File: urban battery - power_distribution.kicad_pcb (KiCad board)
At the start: 2 copper layers, 88.3 x 71.4 mm, 20 parts, among them J1 FRONT_ACC_OUT, J2 12V_IN, J3 12VHC_OUT_EXTRA, J4 TEL_OUT, J5 REAR_ACC_OUT, J6 MTR_CTRL_OUT, J7 12VLC_OUT_EXTRA, J8 12VLC_OUT_EXTRA, J9 12VLC_OUT_EXTRA

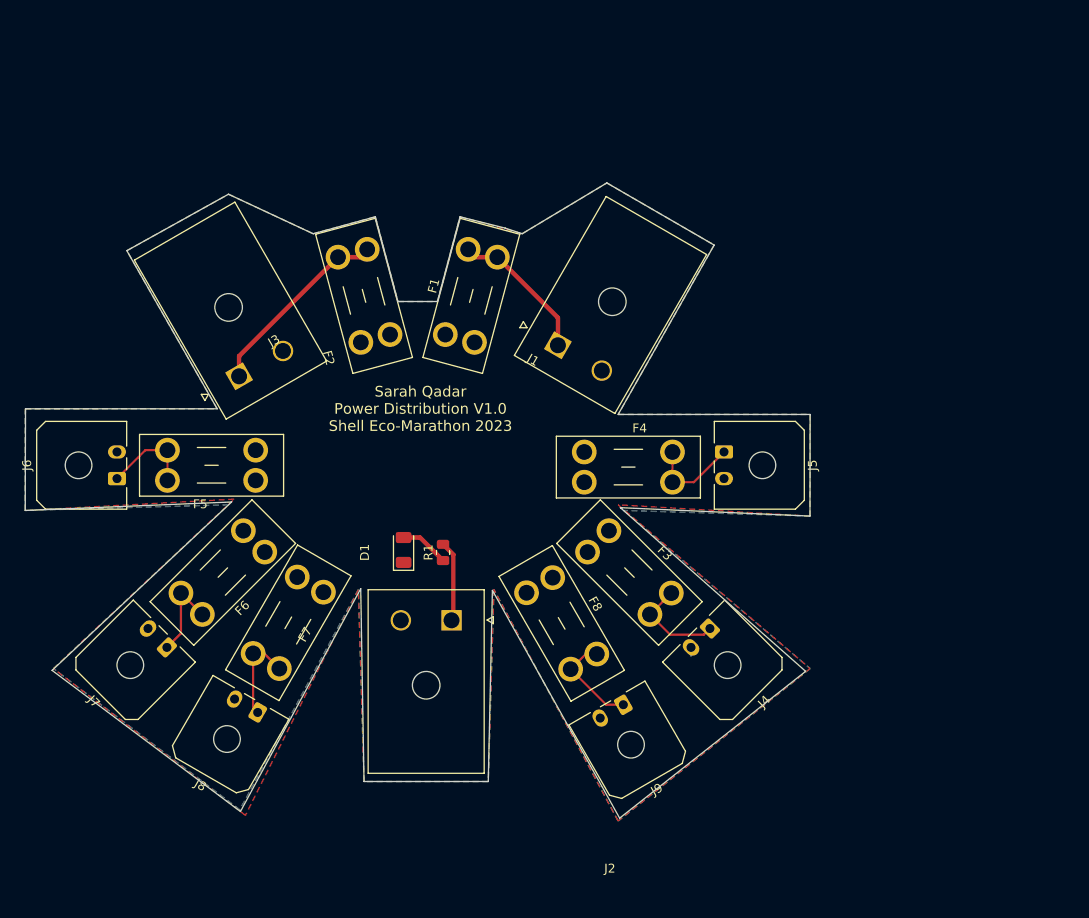
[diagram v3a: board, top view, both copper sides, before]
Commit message: fixed issue od 12V input going through LED
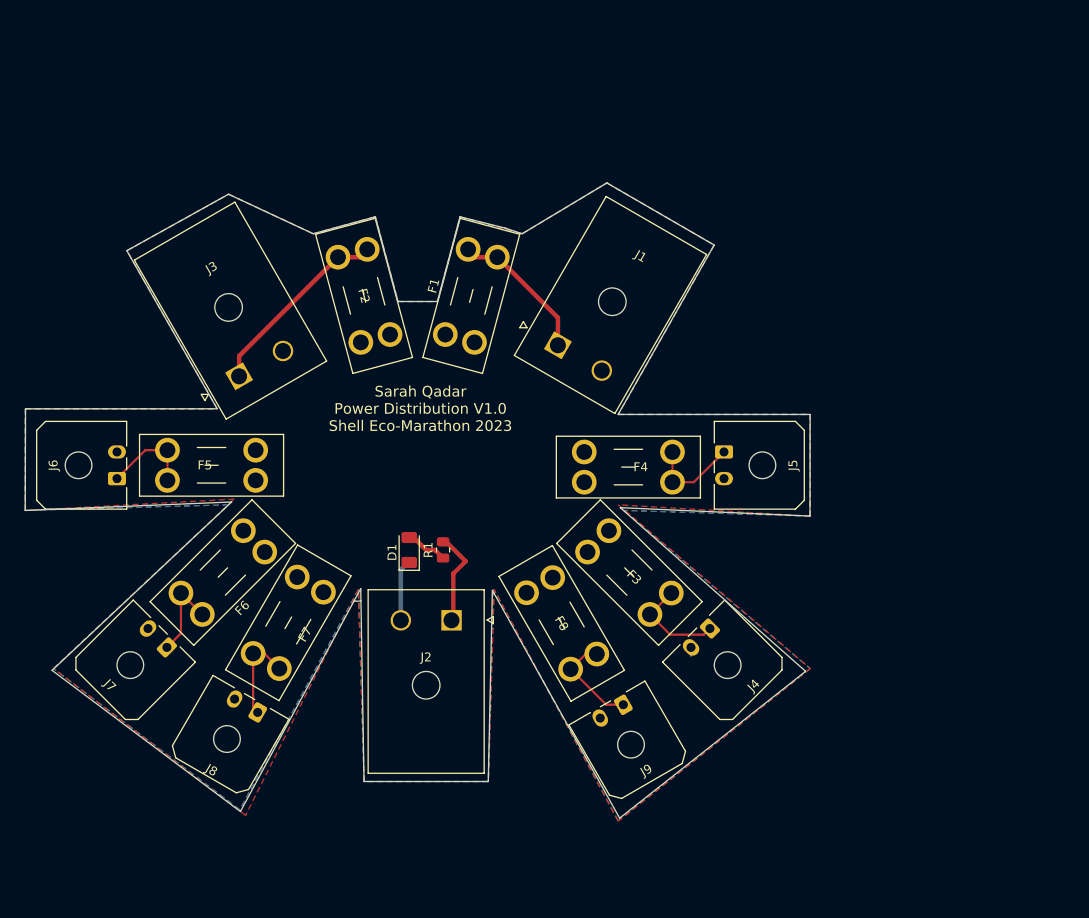
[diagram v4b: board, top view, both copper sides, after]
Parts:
- moved D1 0.64 mm to (114.9, 132.7)
- moved R1 0.28 mm to (118.7, 132.7)
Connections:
- D1 pad 1: +12V -> GND
- J2 pad 1: Net-(J2-Pad1) -> +12V
- R1 pad 2: Net-(J2-Pad1) -> +12V
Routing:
- net +12V: track 0.30 -> 10.7 mm
- net Net-(J2-Pad1): track 9.10 -> 0.00 mm
- net GND: track 0.93 -> 8.69 mm
- net Net-(D1-Pad2): track 5.52 -> 4.77 mm
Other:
- outline, holes or cut-outs redrawn

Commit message: softened sharp inner corners of pcb
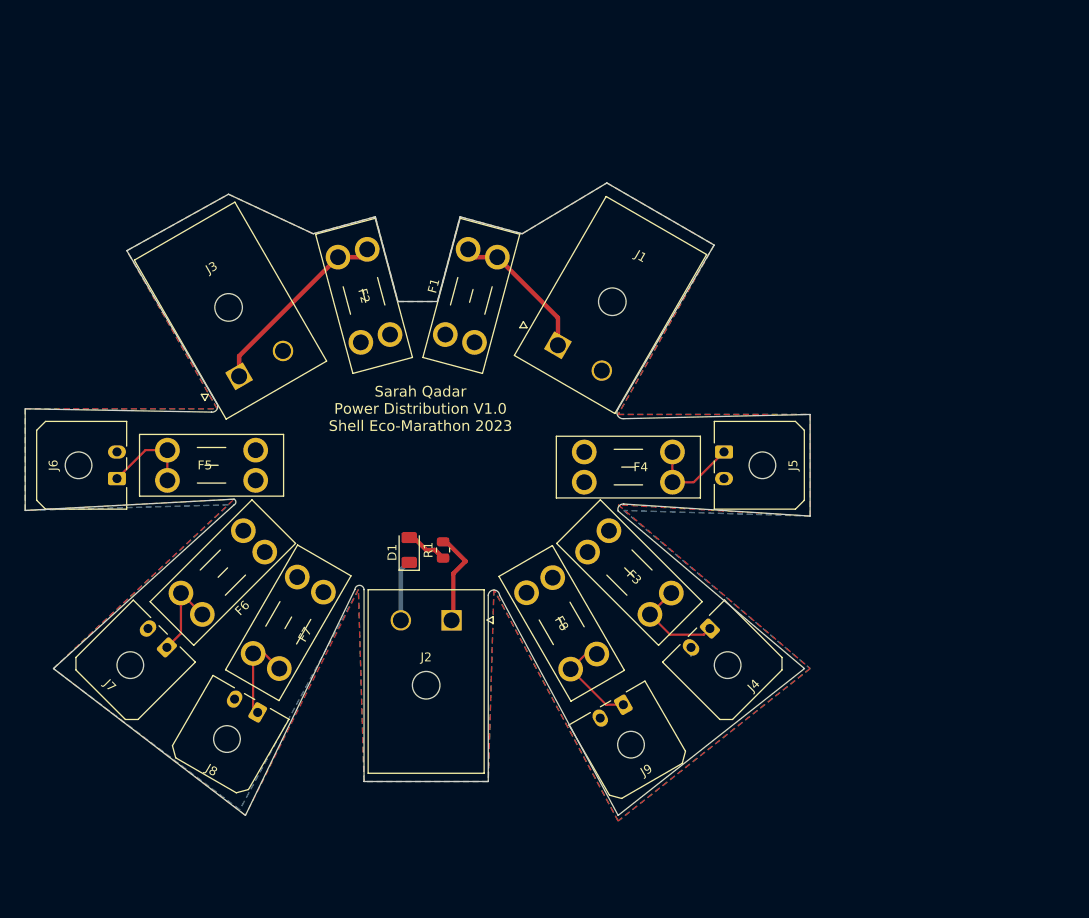
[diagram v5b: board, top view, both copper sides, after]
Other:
- board size 88.3 x 71.4 mm -> 88.3 x 71.1 mm
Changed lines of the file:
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@@
     )
   )
-  (gr_arc (start 109.5 138.43) (mid 109.13 138.479369) (end 108.76 138.43) (layer "Edge.Cuts") (width 0.1))
-  (gr_poly
-    (pts
-      (xy 149.225 98.425)
-      (xy 138.43 117.475)
-      (xy 160.02 117.475)
-      (xy 160.00134 128.904451)
-      (xy 138.675137 127.956526)
-      (xy 159.514361 146.358822)
-      (xy 138.598924 162.868822)
-      (xy 124.289365 137.253849)
-      (xy 123.825 158.75)
-      (xy 109.855 158.75)
-      (xy 109.483669 137.06278)
-      (xy 95.957893 162.127909)
-      (xy 74.777914 146.252909)
-      (xy 94.960553 127.318742)
-      (xy 71.755 128.27)
-      (xy 71.792224 116.84219)
-      (xy 93.345 116.84)
-      (xy 83.185 99.06)
-      (xy 94.615 92.71)
-      (xy 104.14 97.155)
-      (xy 111.125 95.25)
-      (xy 113.665 104.775)
-      (xy 118.11 104.775)
-      (xy 120.65 95.25)
-      (xy 125.73 96.52)
-      (xy 127.635 97.155)
-      (xy 137.16 91.44)
-    ) (layer "Edge.Cuts") (width 0.1) (fill none))
+  (gr_line (start 137.16 91.44) (end 127.635 97.155) (layer "Edge.Cuts") (width 0.1))
+  (gr_line (start 83.185 99.06) (end 93.275606 116.205) (layer "Edge.Cuts") (width 0.1))
+  (gr_line (start 109.855 137.16) (end 109.855 158.75) (layer "Edge.Cuts") (width 0.1))
+  (gr_arc (start 93.275606 116.205) (mid 93.323848 116.89426) (end 92.71 117.21146) (layer "Edge.Cuts") (width 0.1))
+  (gr_line (start 149.225 98.425) (end 137.16 91.44) (layer "Edge.Cuts") (width 0.1))
+  (gr_line (start 159.385 146.05) (end 138.43 128.332923) (layer "Edge.Cuts") (width 0.1))
+  (gr_line (start 160.02 117.475) (end 139.065 117.950101) (layer "Edge.Cuts") (width 0.1))
+  (gr_line (start 71.755 128.27) (end 95.25 127) (layer "Edge.Cuts") (width 0.1))
+  (gr_line (start 120.65 95.25) (end 118.11 104.775) (layer "Edge.Cuts") (width 0.1))
+  (gr_line (start 138.43 162.56) (end 159.385 146.05) (layer "Edge.Cuts") (width 0.1))
+  (gr_line (start 111.125 95.25) (end 104.14 97.155) (layer "Edge.Cuts") (width 0.1))
+  (gr_line (start 125.095 137.795) (end 138.43 162.56) (layer "Edge.Cuts") (width 0.1))
+  (gr_line (start 74.93 146.05) (end 96.52 162.56) (layer "Edge.Cuts") (width 0.1))
+  (gr_arc (start 123.825 137.795) (mid 124.46 137.218212) (end 125.095 137.795) (layer "Edge.Cuts") (width 0.1))
+  (gr_line (start 138.43 116.84) (end 149.225 98.425) (layer "Edge.Cuts") (width 0.1))
+  (gr_line (start 92.71 117.21146) (end 71.755 116.84) (layer "Edge.Cuts") (width 0.1))
+  (gr_arc (start 139.065 117.950101) (mid 138.378248 117.60627) (end 138.43 116.84) (layer "Edge.Cuts") (width 0.1))
+  (gr_line (start 160.02 128.905) (end 160.02 117.475) (layer "Edge.Cuts") (width 0.1))
+  (gr_line (start 71.755 116.84) (end 71.755 128.27) (layer "Edge.Cuts") (width 0.1))
+  (gr_line (start 123.825 158.75) (end 123.825 137.795) (layer "Edge.Cuts") (width 0.1))
+  (gr_line (start 104.14 97.155) (end 94.615 92.71) (layer "Edge.Cuts") (width 0.1))
+  (gr_line (start 118.11 104.775) (end 113.665 104.775) (layer "Edge.Cuts") (width 0.1))
+  (gr_line (start 139.065 127.548376) (end 160.02 128.905) (layer "Edge.Cuts") (width 0.1))
+  (gr_arc (start 95.25 127) (mid 95.446196 127.3175) (end 95.25 127.635) (layer "Edge.Cuts") (width 0.1))
+  (gr_line (start 95.25 127.635) (end 74.93 146.05) (layer "Edge.Cuts") (width 0.1))
+  (gr_line (start 94.615 92.71) (end 83.185 99.06) (layer "Edge.Cuts") (width 0.1))
+  (gr_arc (start 108.828711 137.16) (mid 109.341855 136.691625) (end 109.855 137.16) (layer "Edge.Cuts") (width 0.1))
+  (gr_arc (start 138.43 128.332923) (mid 138.532412 127.766553) (end 139.065 127.548376) (layer "Edge.Cuts") (width 0.1))
+  (gr_line (start 96.52 162.56) (end 108.828711 137.16) (layer "Edge.Cuts") (width 0.1))
+  (gr_line (start 109.855 158.75) (end 123.825 158.75) (layer "Edge.Cuts") (width 0.1))
+  (gr_line (start 113.665 104.775) (end 111.125 95.25) (layer "Edge.Cuts") (width 0.1))
+  (gr_line (start 127.635 97.155) (end 120.65 95.25) (layer "Edge.Cuts") (width 0.1))
   (gr_text "Sarah Qadar\nPower Distribution V1.0\nShell Eco-Marathon 2023" (at 116.205 116.84) (layer "F.SilkS")
     (effects (font (size 1.2 1.2) (thickness 0.3)))
@@
     (polygon
       (pts
-        (xy 149.246275 98.425)
-        (xy 138.451275 117.475)
-        (xy 160.041275 117.475)
-        (xy 160.041275 128.905)
-        (xy 138.451275 127.635)
-        (xy 160.041275 146.05)
-        (xy 138.451275 163.195)
-        (xy 124.481275 137.16)
-        (xy 123.846275 158.75)
-        (xy 109.876275 158.75)
-        (xy 109.241275 137.16)
-        (xy 96.541275 162.56)
-        (xy 74.951275 146.05)
-        (xy 95.271275 127)
-        (xy 71.776275 128.27)
-        (xy 71.776275 116.84)
-        (xy 93.366275 116.84)
-        (xy 83.206275 99.06)
-        (xy 94.636275 92.71)
-        (xy 104.161275 97.155)
-        (xy 111.146275 95.25)
-        (xy 113.686275 104.775)
-        (xy 118.131275 104.775)
-        (xy 120.671275 95.25)
-        (xy 127.656275 97.155)
-        (xy 137.181275 91.44)
+        (xy 149.225 98.425)
+        (xy 138.43 117.475)
+        (xy 160.02 117.475)
+        (xy 160.02 128.905)
+        (xy 138.43 127.635)
+        (xy 160.02 146.05)
+        (xy 138.43 163.195)
+        (xy 124.46 137.16)
+        (xy 123.825 158.75)
+        (xy 109.855 158.75)
+        (xy 109.22 137.16)
+        (xy 96.52 162.56)
+        (xy 74.93 146.05)
+        (xy 95.25 127)
+        (xy 71.755 128.27)
+        (xy 71.755 116.84)
+        (xy 93.345 116.84)
+        (xy 83.185 99.06)
+        (xy 94.615 92.71)
+        (xy 104.14 97.155)
+        (xy 111.125 95.25)
+        (xy 113.665 104.775)
+        (xy 118.11 104.775)
+        (xy 120.65 95.25)
+        (xy 127.635 97.155)
+        (xy 137.16 91.44)
       )
     )

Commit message: pcb routing,added mounting holes and proper labels
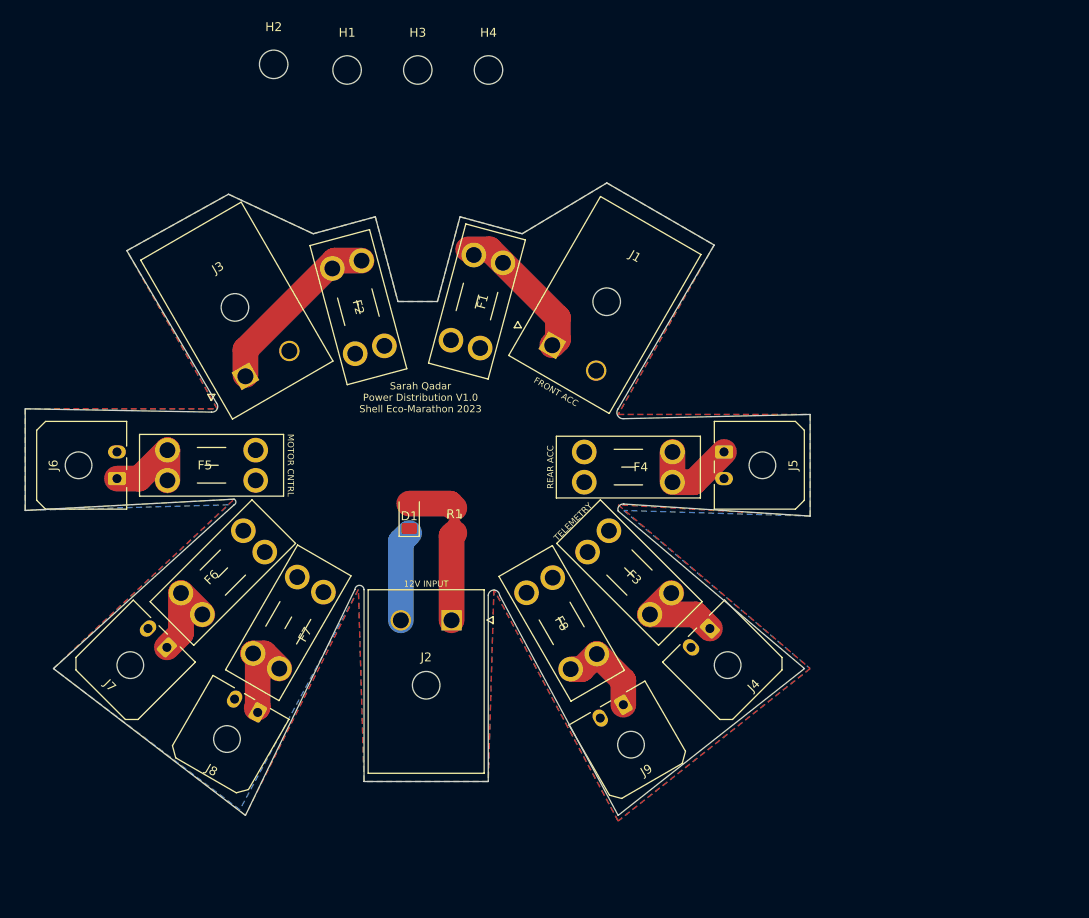
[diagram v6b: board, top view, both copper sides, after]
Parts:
- added H1: MountingHole, MountingHole:MountingHole_3.2mm_M3, F.Cu at (108.0, 78.7)
- added H2: MountingHole, MountingHole:MountingHole_3.2mm_M3, F.Cu at (99.7, 78.1)
- added H3: MountingHole, MountingHole:MountingHole_3.2mm_M3, F.Cu at (115.9, 78.7)
- added H4: MountingHole, MountingHole:MountingHole_3.2mm_M3, F.Cu at (123.8, 78.7)
- J5: value REAR_ACC_OUT -> REAR ACC
- moved R1 4.02 mm to (120.0, 128.9)
- moved D1 3.81 mm to (114.9, 128.9)
- moved G*** 3.24 mm to (116.2, 122.6)
- moved F2 1.42 mm to (108.9, 110.6)
- moved F1 0.90 mm to (119.6, 109.1)
- moved J3 0.71 mm to (96.5, 113.2)
- moved J1 0.64 mm to (131.0, 109.7)
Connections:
- J2 pad 1: +12V -> Net-(D1-Pad2)
- R1 pad 2: +12V -> Net-(D1-Pad2)
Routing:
- net +12V: track 10.7 -> 0.00 mm
- net Net-(D1-Pad2): track 4.77 -> 15.2 mm
- net GND: track 8.69 -> 10.6 mm
- net Net-(F1-Pad2): track 16.4 -> 17.9 mm
- net Net-(F2-Pad2): track 21.7 -> 20.8 mm
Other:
- board text added: "12V INPUT"
- board text added: "FRONT ACC"
- board text added: "MOTOR CNTRL"
- board text added: "TELEMETRY"

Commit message: fixed schematic and layout bugs
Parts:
- removed H3, H4: MountingHole, MountingHole:MountingHole_3.2mm_M3
- J5: value REAR ACC -> REAR_ACC_OUT
- moved H2 47.6 mm to (126.4, 117.5)
- moved H1 38.8 mm to (105.4, 117.5)
- moved R1 4.20 mm to (118.7, 132.9)
- moved D1 4.01 mm to (114.9, 132.9)
- moved G*** 3.81 mm to (116.2, 126.4)
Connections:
- J2 pad 1: Net-(D1-Pad2) -> +12V
- R1 pad 2: Net-(D1-Pad2) -> +12V
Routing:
- net Net-(F2-Pad2): track 20.8 -> 42.4 mm
- net +12V: track 0.00 -> 18.9 mm
- net Net-(F1-Pad2): track 17.9 -> 31.7 mm
- net Net-(D1-Pad2): track 15.2 -> 5.22 mm
- net GND: track 10.6 -> 12.8 mm
- net Net-(F7-Pad2): track 10.6 -> 11.5 mm
